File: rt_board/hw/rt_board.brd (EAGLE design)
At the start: 63.8 x 73.7 mm, 68 parts, among them IC1 MCP170333MB, IC2/L1 TLE4935L, IC3/L2 TLE4935L, IC4/R1 TLE4935L, IC5/R2 TLE4935L, Q1 8MHz, SW1 B3U-1000PM-B, SW2 B3U-1000PM-B, U1 DRV8801PWP, U2 DRV8801PWP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

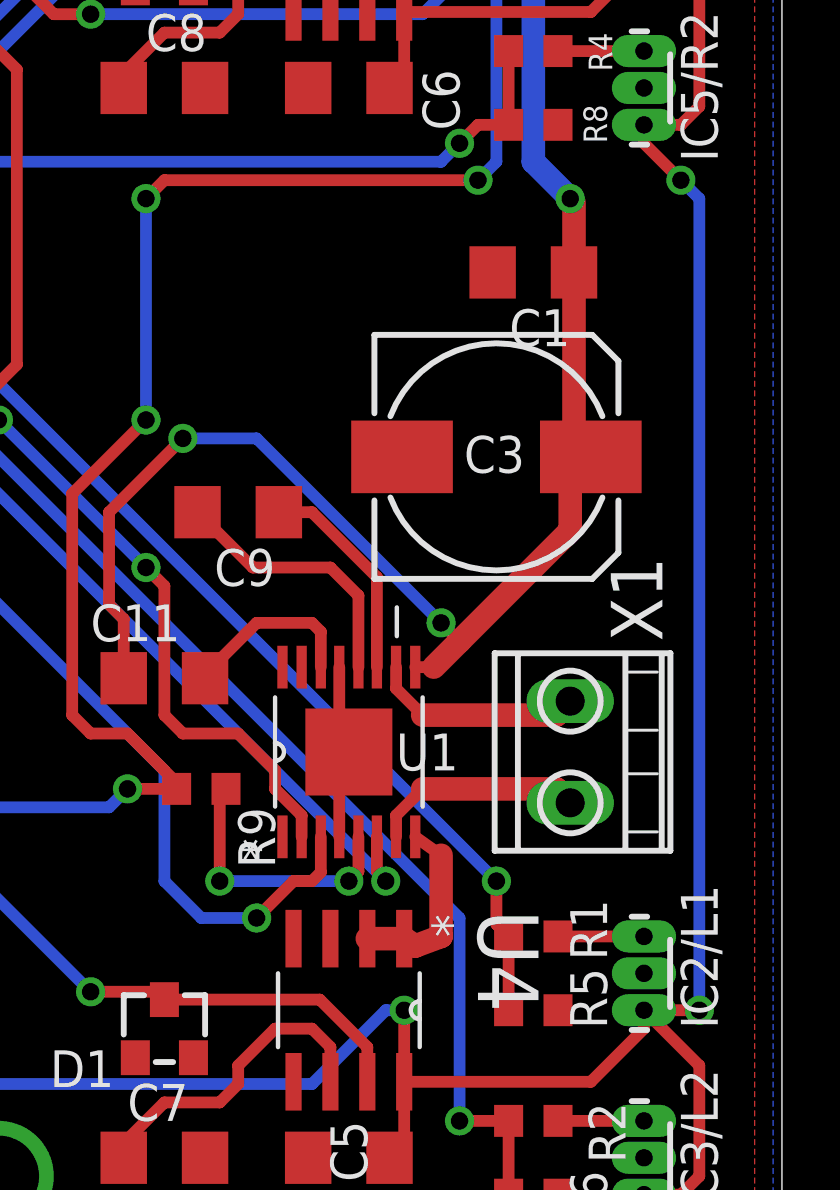
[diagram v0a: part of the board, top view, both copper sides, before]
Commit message: added 4x100nF for Hall sensors
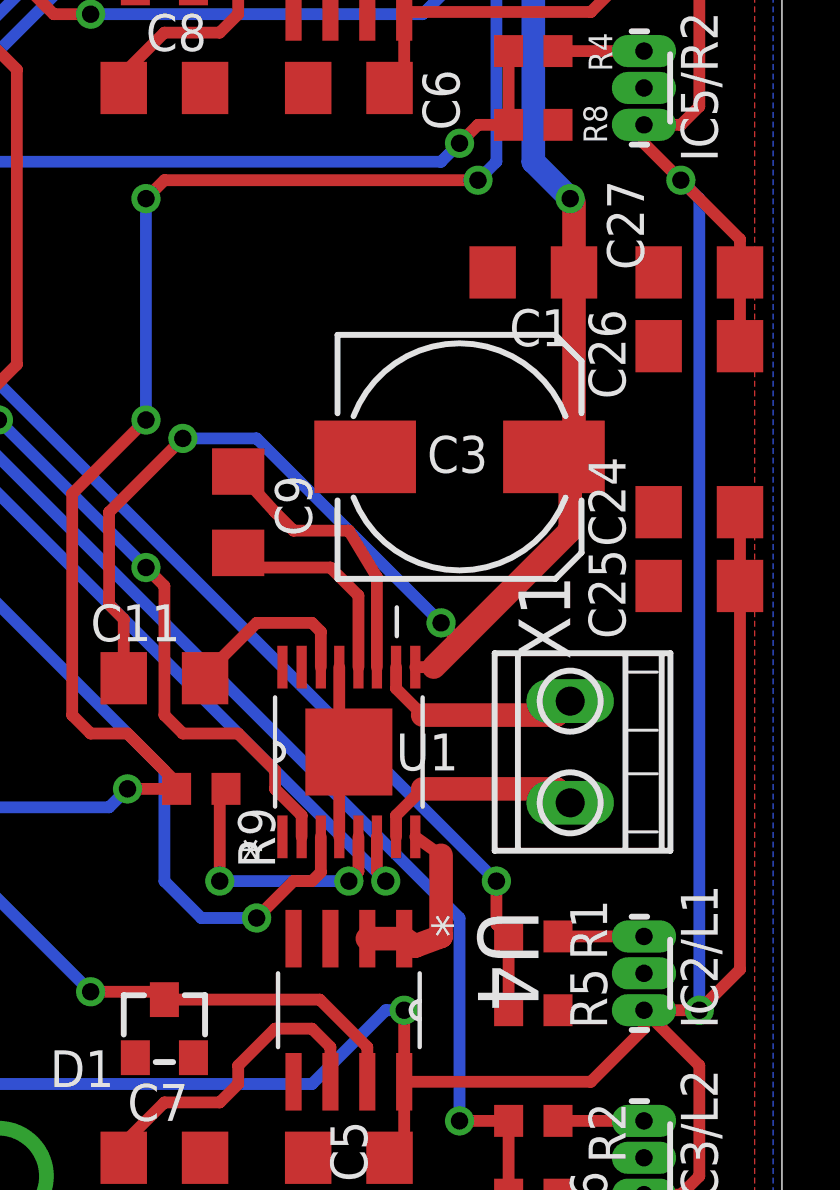
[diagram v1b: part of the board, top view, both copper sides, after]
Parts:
- added C24, C25, C26, C27: 100nF, rcl:C1206
- moved C3 1.27 mm to (63.5, 34.3)
- turned C9 to 270 degrees
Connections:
- net +5V/1: now also C24.1, C25.1, C26.1, C27.1
- net 0V: now also C24.2, C25.2, C26.2, C27.2
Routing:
- net +5V/1: track 142.5 -> 166.8 mm
- net N$28: track 7.40 -> 9.66 mm
- net N$27: track 9.19 -> 7.21 mm
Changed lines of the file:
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@@
 <attribute name="MF" value="" x="67.31" y="24.13" size="1.778" layer="27" rot="R90" display="off"/>
 <attribute name="OC_FARNELL" value="unknown" x="67.31" y="24.13" size="1.778" layer="27" rot="R90" display="off"/>
-<attribute name="NAME" x="70.485" y="27.94" size="1.778" layer="25" rot="R90"/>
+<attribute name="NAME" x="67.31" y="27.305" size="1.778" layer="25" rot="R90"/>
 <attribute name="VALUE" x="73.025" y="20.955" size="1.778" layer="27" rot="R90"/>
 </element>
@@
 </element>
 <element name="C1" library="rcl" package="C1206" value="100nF" x="66.04" y="40.64" rot="R180"/>
-<element name="C3" library="rcl" package="153CLV-0810" value="100uF" x="64.77" y="34.29" smashed="yes">
-<attribute name="NAME" x="63.655" y="33.74" size="1.27" layer="25"/>
-<attribute name="VALUE" x="62.35" y="31.045" size="1.27" layer="27"/>
+<element name="C3" library="rcl" package="153CLV-0810" value="100uF" x="63.5" y="34.29" smashed="yes">
+<attribute name="NAME" x="62.385" y="33.74" size="1.27" layer="25"/>
+<attribute name="VALUE" x="61.08" y="31.045" size="1.27" layer="27"/>
 </element>
 <element name="U4" library="Allegro-ACS712ELCTR-20A-T" package="SOIC127P600X175-8N" value="ACS712ELCTR-05B-T" x="59.69" y="15.24" smashed="yes" rot="R270">
@@
 <attribute name="VALUE" x="50.8" y="24.13" size="1.27" layer="27"/>
 </element>
-<element name="C9" library="rcl" package="C1206" value="100nF" x="55.88" y="32.385" rot="R180"/>
+<element name="C9" library="rcl" package="C1206" value="100nF" x="55.88" y="32.385" rot="R270"/>
 <element name="IC4/R1" library="allegro" package="SIP3-UA" value="TLE4935L" x="69.85" y="53.34" smashed="yes" rot="R90">
 <attribute name="OC_NEWARK" value="unknown" x="30.48" y="53.34" size="1.778" layer="27" rot="R90" display="off"/>
@@
 <attribute name="NAME" x="42.335" y="64.585" size="1.27" layer="25"/>
 <attribute name="VALUE" x="38.49" y="56.08" size="1.27" layer="27"/>
+</element>
+<element name="C24" library="rcl" package="C1206" value="100nF" x="71.755" y="32.385" smashed="yes" rot="R180">
+<attribute name="NAME" x="67.945" y="34.29" size="1.27" layer="25" rot="R270"/>
+<attribute name="VALUE" x="73.66" y="34.925" size="1.27" layer="27" rot="R180"/>
+</element>
+<element name="C25" library="rcl" package="C1206" value="100nF" x="71.755" y="29.845" smashed="yes" rot="R180">
+<attribute name="NAME" x="67.945" y="31.115" size="1.27" layer="25" rot="R270"/>
+<attribute name="VALUE" x="73.66" y="28.575" size="1.27" layer="27" rot="R180"/>
+</element>
+<element name="C26" library="rcl" package="C1206" value="100nF" x="71.755" y="38.1" smashed="yes" rot="R180">
+<attribute name="NAME" x="67.945" y="39.37" size="1.27" layer="25" rot="R270"/>
+<attribute name="VALUE" x="73.66" y="36.83" size="1.27" layer="27" rot="R180"/>
+</element>
+<element name="C27" library="rcl" package="C1206" value="100nF" x="71.755" y="40.64" smashed="yes" rot="R180">
+<attribute name="NAME" x="68.58" y="43.815" size="1.27" layer="25" rot="R270"/>
+<attribute name="VALUE" x="74.295" y="43.18" size="1.27" layer="27" rot="R180"/>
 </element>
 </elements>
@@
 <wire x1="36.195" y1="60.325" x2="37.68" y2="58.84" width="0.4064" layer="1"/>
 <contactref element="C23" pad="-"/>
+<contactref element="C26" pad="2"/>
+<contactref element="C27" pad="2"/>
+<contactref element="C25" pad="2"/>
+<contactref element="C24" pad="2"/>
 </signal>
 <signal name="+5V">
@@
 <wire x1="67.31" y1="31.75" x2="67.31" y2="33.58" width="0.8128" layer="1"/>
 <wire x1="67.31" y1="33.58" x2="67.665" y2="33.935" width="0.4064" layer="1"/>
-<wire x1="67.665" y1="33.935" x2="68.02" y2="34.29" width="0.4064" layer="1"/>
+<wire x1="67.665" y1="33.935" x2="66.75" y2="34.29" width="0.4064" layer="1"/>
 <wire x1="67.44" y1="40.64" x2="67.44" y2="34.16" width="0.8128" layer="1"/>
 <wire x1="67.44" y1="34.16" x2="67.665" y2="33.935" width="0.4064" layer="1"/>
@@
 <wire x1="18.255" y1="13.97" x2="18.415" y2="13.97" width="0.4064" layer="1"/>
 <wire x1="18.415" y1="13.97" x2="18.415" y2="18.415" width="0.4064" layer="1"/>
+<contactref element="C27" pad="1"/>
+<contactref element="C26" pad="1"/>
+<contactref element="C24" pad="1"/>
+<contactref element="C25" pad="1"/>
+<wire x1="73.155" y1="40.64" x2="73.155" y2="38.1" width="0.4064" layer="1"/>
+<wire x1="73.155" y1="40.64" x2="73.155" y2="41.78" width="0.4064" layer="1"/>
+<wire x1="73.155" y1="41.78" x2="71.12" y2="43.815" width="0.4064" layer="1"/>
+<wire x1="73.155" y1="29.845" x2="73.155" y2="16.64" width="0.4064" layer="1"/>
+<wire x1="73.155" y1="16.64" x2="71.755" y2="15.24" width="0.4064" layer="1"/>
+<wire x1="73.155" y1="32.385" x2="73.155" y2="29.845" width="0.4064" layer="1"/>
 </signal>
 <signal name="N$11">
@@
 <wire x1="60.0202" y1="29.5148" x2="59.055" y2="30.48" width="0.4064" layer="1"/>
 <wire x1="59.055" y1="30.48" x2="56.385" y2="30.48" width="0.4064" layer="1"/>
-<wire x1="56.385" y1="30.48" x2="54.48" y2="32.385" width="0.4064" layer="1"/>
+<wire x1="56.385" y1="30.48" x2="55.88" y2="30.985" width="0.4064" layer="1"/>
 </signal>
 <signal name="N$28">
@@
 <contactref element="C9" pad="1"/>
 <wire x1="60.6552" y1="27.051" x2="60.6552" y2="30.1498" width="0.4064" layer="1"/>
-<wire x1="60.6552" y1="30.1498" x2="58.42" y2="32.385" width="0.4064" layer="1"/>
-<wire x1="58.42" y1="32.385" x2="57.28" y2="32.385" width="0.4064" layer="1"/>
+<wire x1="60.6552" y1="30.1498" x2="59.69" y2="31.75" width="0.4064" layer="1"/>
+<wire x1="59.69" y1="31.75" x2="57.785" y2="31.75" width="0.4064" layer="1"/>
+<wire x1="57.785" y1="31.75" x2="57.15" y2="32.385" width="0.4064" layer="1"/>
+<wire x1="57.15" y1="32.385" x2="55.88" y2="33.785" width="0.4064" layer="1"/>
 </signal>
 <signal name="N$29">

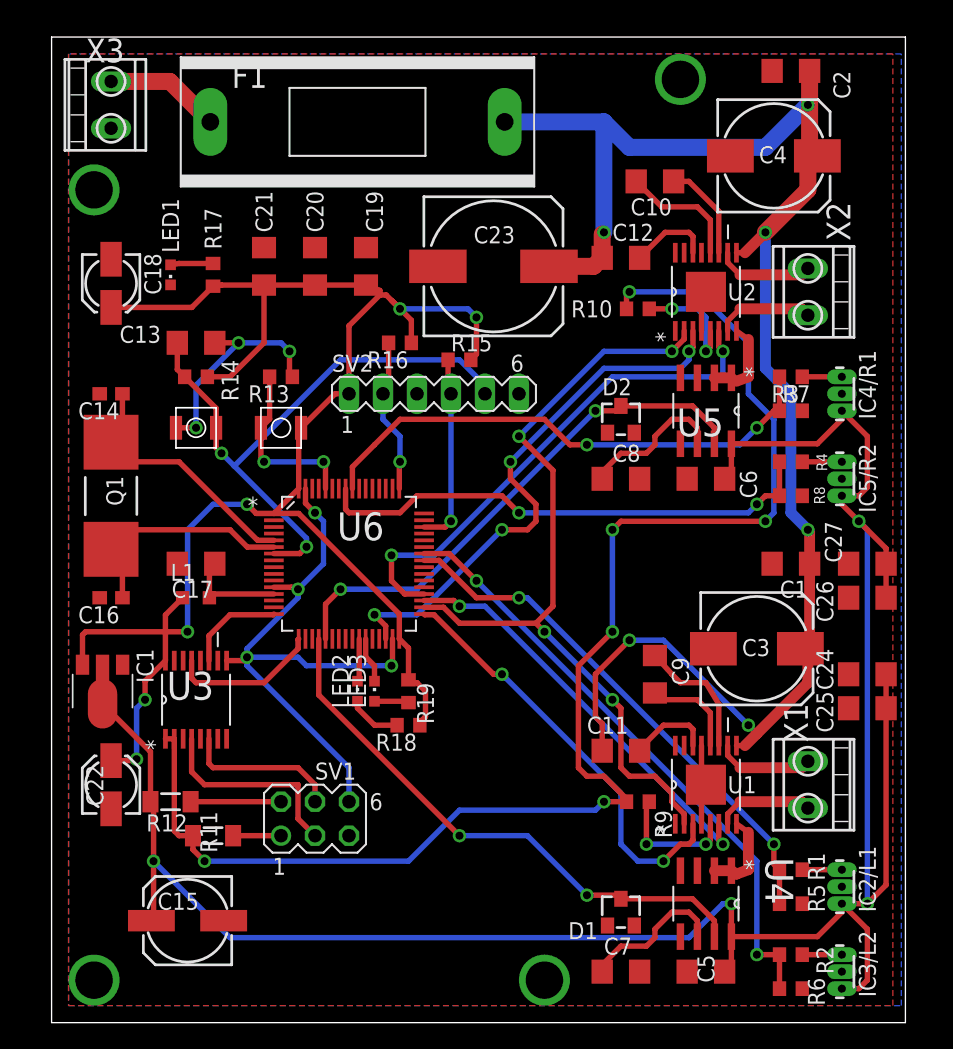
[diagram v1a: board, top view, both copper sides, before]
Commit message: replaced power connectors with the ones of an aproperiate size
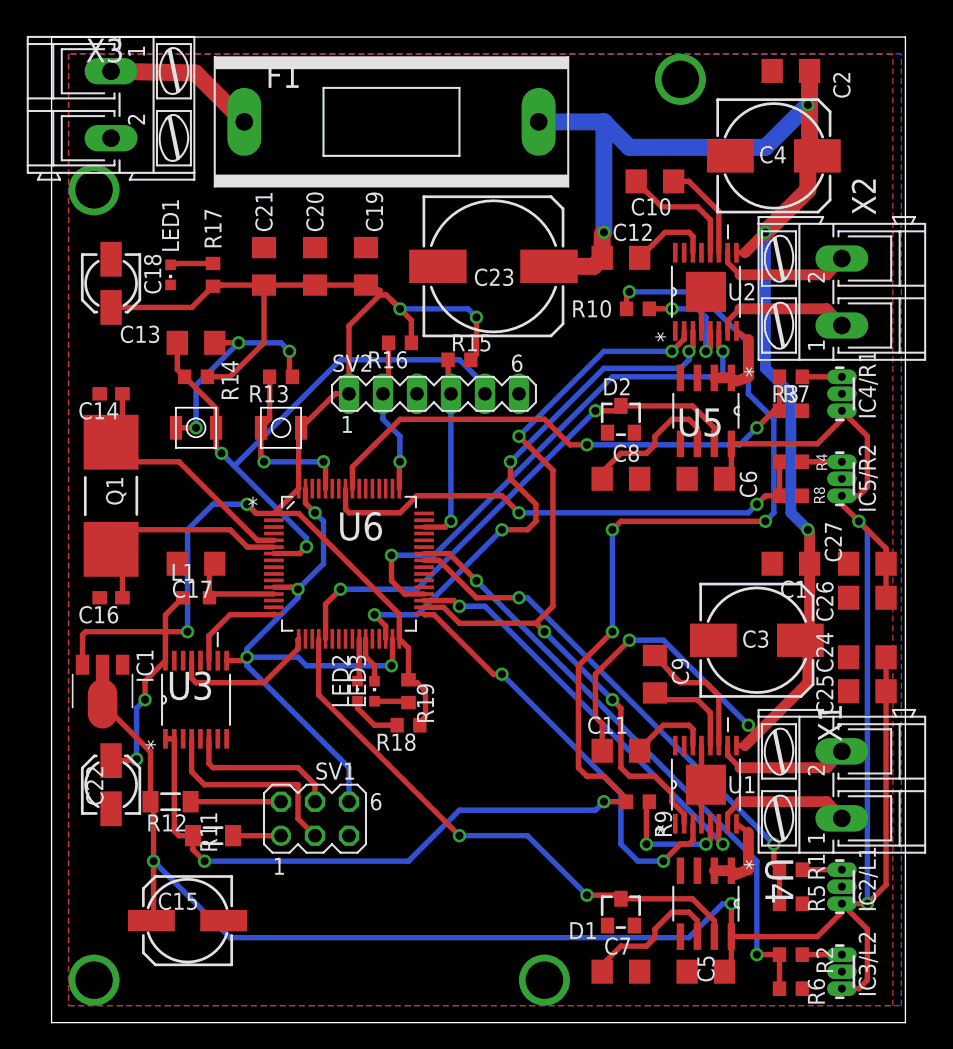
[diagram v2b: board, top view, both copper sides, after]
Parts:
- X1, X2, X3: device con-ptr500:AK550/2 -> con-ptr500:AK300/2
- moved F1 2.54 mm to (36.2, 73.7)
- moved X1 2.54 mm to (69.8, 24.1)
- moved X2 2.54 mm to (69.8, 61.0)
- moved C24 1.27 mm to (71.8, 33.7)
- moved C25 1.27 mm to (71.8, 31.1)
- moved C3 0.63 mm to (63.5, 34.9)
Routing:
- net N$33: track 7.31 -> 10.2 mm
- net N$20: track 7.31 -> 10.2 mm
- net N$21: track 7.31 -> 10.2 mm
- net N$34: track 7.31 -> 10.2 mm
- net N$2: track 8.67 -> 11.5 mm
- net +12V: track 122.5 -> 120.4 mm
- net +5V/1: track 166.8 -> 168.0 mm
